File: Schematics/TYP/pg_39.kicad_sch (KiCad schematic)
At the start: 35 parts

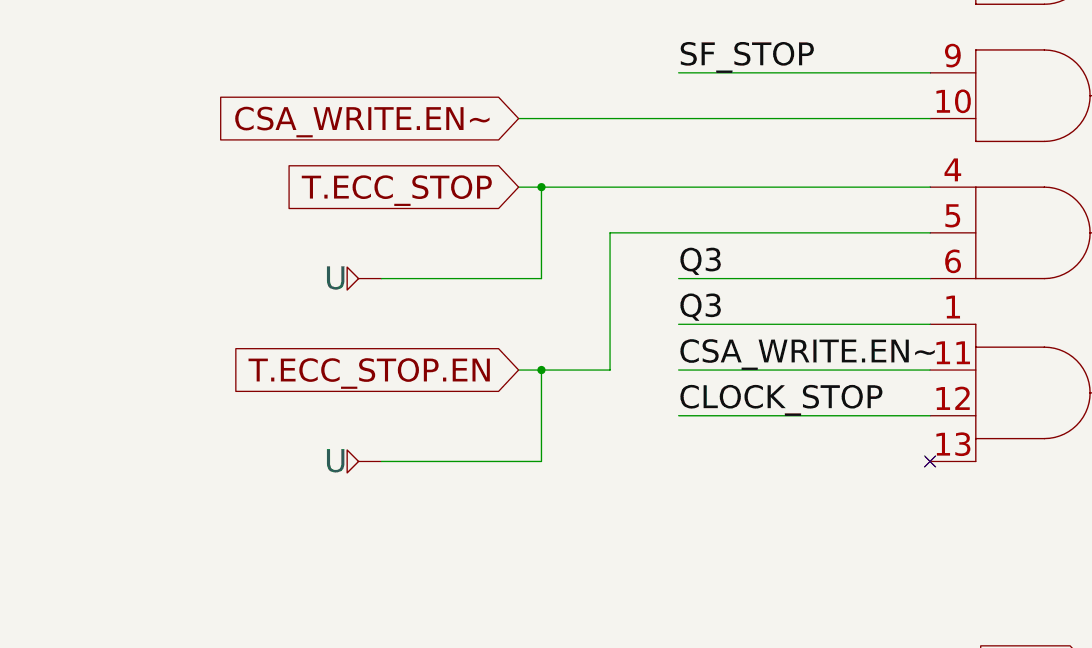
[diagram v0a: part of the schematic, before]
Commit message: ECC removal cleanup
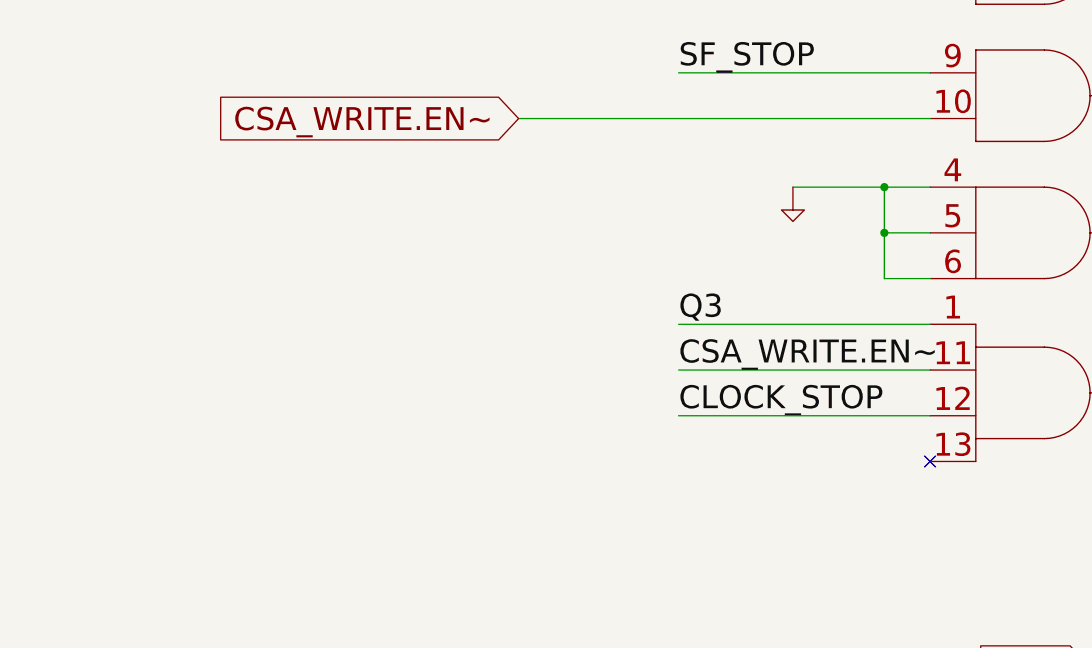
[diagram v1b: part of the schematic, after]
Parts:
- removed U (x2): (no value), symbol r1000:GB
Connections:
- net T.ECC_STOP is gone; now on net PD: U.4 (C0)
- net T.ECC_STOP.EN is gone; now on net PD: U.5 (C1)
- net PD: now also U.6 (C2)
- net Q3: no longer U.6 (C2)
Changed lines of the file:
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@@
     (comment 4 "RELEASED")
   )
+  (junction (at 124.46 241.3) (diameter 0) (color 0 0 0 0)
+  )
   (junction (at 215.9 205.74) (diameter 0) (color 0 0 0 0)
   )
@@
   (junction (at 124.46 93.98) (diameter 0) (color 0 0 0 0)
   )
-  (junction (at 86.36 241.3) (diameter 0) (color 0 0 0 0)
-  )
   (junction (at 424.18 40.64) (diameter 0) (color 0 0 0 0)
   )
@@
   (junction (at 182.88 104.14) (diameter 0) (color 0 0 0 0)
   )
+  (junction (at 124.46 246.38) (diameter 0) (color 0 0 0 0)
+  )
   (junction (at 182.88 238.76) (diameter 0) (color 0 0 0 0)
-  )
-  (junction (at 86.36 261.62) (diameter 0) (color 0 0 0 0)
   )
   (junction (at 469.9 48.26) (diameter 0) (color 0 0 0 0)
@@
     (stroke (width 0) (type default))
   )
-  (wire (pts (xy 129.54 246.38) (xy 93.98 246.38))
-    (stroke (width 0) (type default))
-  )
   (wire (pts (xy 63.5 27.94) (xy 78.74 27.94))
     (stroke (width 0) (type default))
@@
     (stroke (width 0) (type default))
   )
-  (wire (pts (xy 86.36 261.62) (xy 86.36 271.78))
-    (stroke (width 0) (type default))
-  )
   (wire (pts (xy 208.28 218.44) (xy 215.9 218.44))
     (stroke (width 0) (type default))
@@
     (stroke (width 0) (type default))
   )
-  (wire (pts (xy 86.36 241.3) (xy 129.54 241.3))
-    (stroke (width 0) (type default))
-  )
   (wire (pts (xy 424.18 96.52) (xy 431.8 96.52))
     (stroke (width 0) (type default))
@@
     (stroke (width 0) (type default))
   )
+  (wire (pts (xy 124.46 241.3) (xy 129.54 241.3))
+    (stroke (width 0) (type default))
+  )
   (wire (pts (xy 454.66 99.06) (xy 477.52 99.06))
     (stroke (width 0) (type default))
@@
     (stroke (width 0) (type default))
   )
-  (wire (pts (xy 101.6 251.46) (xy 129.54 251.46))
-    (stroke (width 0) (type default))
-  )
   (wire (pts (xy 147.32 294.64) (xy 154.94 294.64))
     (stroke (width 0) (type default))
@@
     (stroke (width 0) (type default))
   )
-  (wire (pts (xy 68.58 271.78) (xy 86.36 271.78))
-    (stroke (width 0) (type default))
-  )
   (wire (pts (xy 350.52 314.96) (xy 350.52 345.44))
     (stroke (width 0) (type default))
@@
     (stroke (width 0) (type default))
   )
-  (wire (pts (xy 68.58 251.46) (xy 86.36 251.46))
-    (stroke (width 0) (type default))
-  )
   (wire (pts (xy 182.88 83.82) (xy 182.88 104.14))
     (stroke (width 0) (type default))
@@
     (stroke (width 0) (type default))
   )
+  (wire (pts (xy 129.54 246.38) (xy 124.46 246.38))
+    (stroke (width 0) (type default))
+  )
   (wire (pts (xy 340.36 345.44) (xy 350.52 345.44))
     (stroke (width 0) (type default))
@@
     (stroke (width 0) (type default))
   )
-  (wire (pts (xy 86.36 261.62) (xy 83.82 261.62))
-    (stroke (width 0) (type default))
-  )
   (wire (pts (xy 154.94 297.18) (xy 154.94 294.64))
     (stroke (width 0) (type default))
   )
+  (wire (pts (xy 124.46 251.46) (xy 124.46 246.38))
+    (stroke (width 0) (type default))
+  )
   (wire (pts (xy 170.18 294.64) (xy 162.56 294.64))
     (stroke (width 0) (type default))
@@
     (stroke (width 0) (type default))
   )
-  (wire (pts (xy 93.98 246.38) (xy 93.98 261.62))
-    (stroke (width 0) (type default))
-  )
   (wire (pts (xy 215.9 205.74) (xy 124.46 205.74))
     (stroke (width 0) (type default))
@@
     (stroke (width 0) (type default))
   )
-  (wire (pts (xy 93.98 261.62) (xy 86.36 261.62))
+  (wire (pts (xy 129.54 251.46) (xy 124.46 251.46))
     (stroke (width 0) (type default))
   )
@@
     (stroke (width 0) (type default))
   )
+  (wire (pts (xy 124.46 246.38) (xy 124.46 241.3))
+    (stroke (width 0) (type default))
+  )
   (wire (pts (xy 353.06 309.88) (xy 353.06 340.36))
     (stroke (width 0) (type default))
@@
     (stroke (width 0) (type default))
   )
-  (wire (pts (xy 86.36 251.46) (xy 86.36 241.3))
-    (stroke (width 0) (type default))
-  )
   (wire (pts (xy 381 134.62) (xy 421.64 134.62))
     (stroke (width 0) (type default))
@@
     (stroke (width 0) (type default))
   )
-  (wire (pts (xy 83.82 241.3) (xy 86.36 241.3))
-    (stroke (width 0) (type default))
-  )
   (wire (pts (xy 294.64 124.46) (xy 302.26 124.46))
     (stroke (width 0) (type default))
@@
     (stroke (width 0) (type default))
   )
+  (wire (pts (xy 114.3 241.3) (xy 124.46 241.3))
+    (stroke (width 0) (type default))
+  )
   (wire (pts (xy 127 332.74) (xy 142.24 332.74))
     (stroke (width 0) (type default))
@@
   )
   (label "STATE_STOP~" (at 187.96 104.14 0) (fields_autoplaced)
-    (effects (font (size 2.54 2.54)) (justify left bottom))
-  )
-  (label "Q3" (at 101.6 251.46 0) (fields_autoplaced)
     (effects (font (size 2.54 2.54)) (justify left bottom))
   )
@@
     )
   )
-  (global_label "T.ECC_STOP.EN" (shape input) (at 83.82 261.62 180) (fields_autoplaced)
-    (effects (font (size 2.54 2.54)) (justify right))
-    (property "Intersheet References" "${INTERSHEET_REFS}" (id 0) (at 50.8121 261.4613 0)
-      (effects (font (size 1.905 1.905)) (justify right))
-    )
-  )
   (global_label "OF~.SCLK" (shape output) (at 510.54 45.72 0) (fields_autoplaced)
     (effects (font (size 2.54 2.54)) (justify left))
@@
     (effects (font (size 2.54 2.54)) (justify right))
     (property "Intersheet References" "${INTERSHEET_REFS}" (id 0) (at 97.9321 312.2613 0)
-      (effects (font (size 1.905 1.905)) (justify right))
-    )
-  )
-  (global_label "T.ECC_STOP" (shape input) (at 83.82 241.3 180) (fields_autoplaced)
-    (effects (font (size 2.54 2.54)) (justify right))
-    (property "Intersheet References" "${INTERSHEET_REFS}" (id 0) (at 56.9807 241.1413 0)
       (effects (font (size 1.905 1.905)) (justify right))
     )
@@
     (pin "6")
   )
-  (symbol (lib_id "r1000:GB") (at 68.58 251.46 0) (mirror y) (unit 1)
-    (in_bom yes) (on_board yes)
-    (default_instance (reference "U") (unit 1) (value "") (footprint ""))
-    (property "Reference" "U" (id 0) (at 64.77 251.46 0)
-      (effects (font (size 2.54 2.54)) (justify left))
-    )
-    (property "Value" "" (id 1) (at 68.58 251.46 0)
-      (effects (font (size 1.27 1.27)) hide)
-    )
-    (property "Footprint" "" (id 2) (at 68.58 251.46 0)
-      (effects (font (size 1.27 1.27)) hide)
-    )
-    (property "Datasheet" "" (id 3) (at 68.58 251.46 0)
-      (effects (font (size 1.27 1.27)) hide)
-    )
-    (pin "1")
-  )
   (symbol (lib_id "r1000:GB") (at 340.36 355.6 0) (mirror y) (unit 1)
     (in_bom yes) (on_board yes)
@@
     )
     (property "Datasheet" "" (id 3) (at 340.36 350.52 0)
-      (effects (font (size 1.27 1.27)) hide)
-    )
-    (pin "1")
-  )
-  (symbol (lib_id "r1000:GB") (at 68.58 271.78 0) (mirror y) (unit 1)
-    (in_bom yes) (on_board yes)
-    (default_instance (reference "U") (unit 1) (value "") (footprint ""))
-    (property "Reference" "U" (id 0) (at 64.77 271.78 0)
-      (effects (font (size 2.54 2.54)) (justify left))
-    )
-    (property "Value" "" (id 1) (at 68.58 271.78 0)
-      (effects (font (size 1.27 1.27)) hide)
-    )
-    (property "Footprint" "" (id 2) (at 68.58 271.78 0)
-      (effects (font (size 1.27 1.27)) hide)
-    )
-    (property "Datasheet" "" (id 3) (at 68.58 271.78 0)
       (effects (font (size 1.27 1.27)) hide)
     )
@@
       (effects (font (size 1.27 1.27)) hide)
     )
+    (pin "1")
+  )
+  (symbol (lib_id "r1000:PD") (at 114.3 241.3 0) (unit 1)
+    (in_bom no) (on_board yes)
+    (default_instance (reference "U") (unit 1) (value "") (footprint ""))
+    (property "Reference" "U" (id 0) (at 114.3 241.3 0)
+      (effects (font (size 1.27 1.27)) hide)
+    )
+    (property "Value" "" (id 1) (at 114.3 241.3 0)
+      (effects (font (size 1.27 1.27)) hide)
+    )
+    (property "Footprint" "" (id 2) (at 114.3 241.3 0)
+      (effects (font (size 1.27 1.27)) hide)
+    )
+    (property "Datasheet" "" (id 3) (at 114.3 241.3 0)
+      (effects (font (size 1.27 1.27)) hide)
+    )

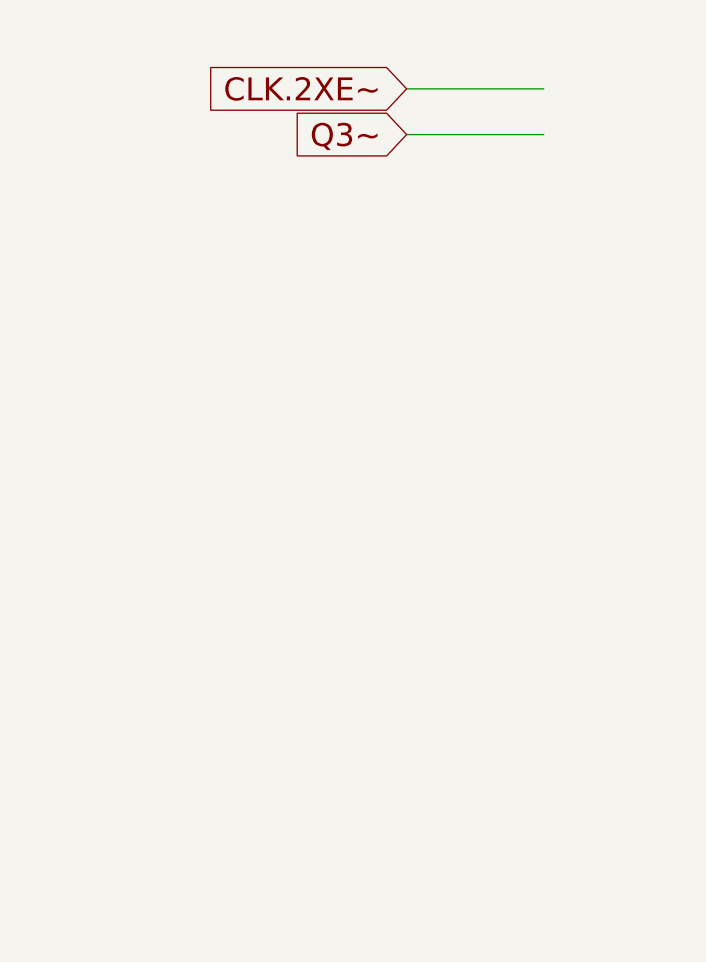
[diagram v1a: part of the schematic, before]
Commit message: Delete blank sheets
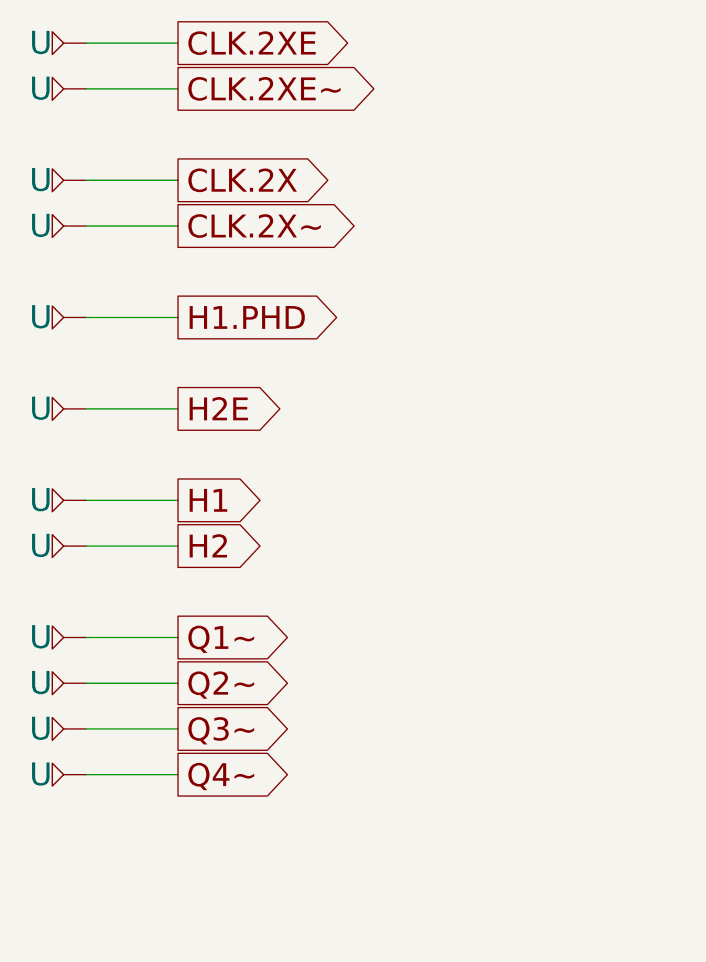
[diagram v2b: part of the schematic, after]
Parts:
- added U (x12): (no value), symbol r1000:GB
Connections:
- net CLK.2XE~: now also U.1
- net H1: now also U.1
- net H2: now also U.1
- net H2E: now also U.1
- net Q2~: now also U.1
- net Q3~: now also U.1
- new net CLK.2X: U.1
- new net CLK.2XE: U.1
- new net CLK.2X~: U.1
- new net H1.PHD: U.1
- new net Q1~: U.1
- new net Q4~: U.1

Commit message: Polish XRF-B symbols, tested to 2.12s (rc051)
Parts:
- added GB: GB, symbol r1000:GB
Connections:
- new net MQ2: GB.1
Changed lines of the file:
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@@
+    (stroke (width 0) (type default))
+  )
+  (wire (pts (xy 38.1 114.3) (xy 27.94 114.3))
     (stroke (width 0) (type default))
   )
@@
     (property "Intersheet References" "${INTERSHEET_REFS}" (id 0) (at 51.054 233.5213 0)
       (effects (font (size 1.905 1.905)) (justify right))
+    )
+  )
+  (global_label "MQ2" (shape output) (at 38.1 114.3 0) (fields_autoplaced)
+    (effects (font (size 2.54 2.54)) (justify left))
+    (property "Intersheetrefs" "${INTERSHEET_REFS}" (id 0) (at 51.5758 114.3 0)
+      (effects (font (size 1.27 1.27)) (justify left))
     )
   )
@@
       (effects (font (size 1.27 1.27)) hide)
     )
+    (pin "1")
+  )
+  (symbol (lib_id "r1000:GB") (at 27.94 114.3 0) (mirror y) (unit 1)
+    (in_bom yes) (on_board yes)
+    (default_instance (reference "GB") (unit 1) (value "GB") (footprint ""))
+    (property "Reference" "GB" (id 0) (at 24.13 114.3 0)
+      (effects (font (size 2.54 2.54)) (justify left))
+    )
+    (property "Value" "GB" (id 1) (at 27.94 114.3 0)
+      (effects (font (size 1.27 1.27)) hide)
+    )
+    (property "Footprint" "" (id 2) (at 27.94 114.3 0)
+      (effects (font (size 1.27 1.27)) hide)
+    )
+    (property "Datasheet" "" (id 3) (at 27.94 114.3 0)
+      (effects (font (size 1.27 1.27)) hide)
+    )

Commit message: TYP: RFA -CS tested to 1.55s (rc055)
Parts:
- removed U: (no value), symbol r1000:GB
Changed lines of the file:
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@@
-    (stroke (width 0) (type default))
-  )
-  (wire (pts (xy 27.94 53.34) (xy 38.1 53.34))
     (stroke (width 0) (type default))
   )
@@
     (property "Intersheet References" "${INTERSHEET_REFS}" (id 0) (at 85.3531 350.3613 0)
       (effects (font (size 1.905 1.905)) (justify right))
-    )
-  )
-  (global_label "H1.PHD" (shape output) (at 38.1 53.34 0) (fields_autoplaced)
-    (effects (font (size 2.54 2.54)) (justify left))
-    (property "Intersheet References" "${INTERSHEET_REFS}" (id 0) (at 56.766 53.1813 0)
-      (effects (font (size 1.905 1.905)) (justify left))
     )
   )
@@
       (effects (font (size 1.27 1.27)) hide)
     )
-    (pin "1")
-  )
-  (symbol (lib_id "r1000:GB") (at 27.94 53.34 0) (mirror y) (unit 1)
-    (in_bom yes) (on_board yes)
-    (default_instance (reference "U") (unit 1) (value "") (footprint ""))
-    (property "Reference" "U" (id 0) (at 24.13 53.34 0)
-      (effects (font (size 2.54 2.54)) (justify left))
-    )
-    (property "Value" "" (id 1) (at 27.94 53.34 0)
-      (effects (font (size 1.27 1.27)) hide)
-    )
-    (property "Footprint" "" (id 2) (at 27.94 53.34 0)
-      (effects (font (size 1.27 1.27)) hide)
-    )
-    (property "Datasheet" "" (id 3) (at 27.94 53.34 0)
-      (effects (font (size 1.27 1.27)) hide)
-    )
